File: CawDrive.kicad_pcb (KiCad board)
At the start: 4 copper layers, 40 x 40 mm, 81 parts, among them J1 Conn_01x11_Pin, J4 Conn_01x07_Pin, Q10 TPH3R704PL, Q11 TPH3R704PL, Q12 TPH3R704PL, Q7 TPH3R704PL, Q8 TPH3R704PL, Q9 TPH3R704PL, U1 STM32F446RETx, U2 TLV76733DRVR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

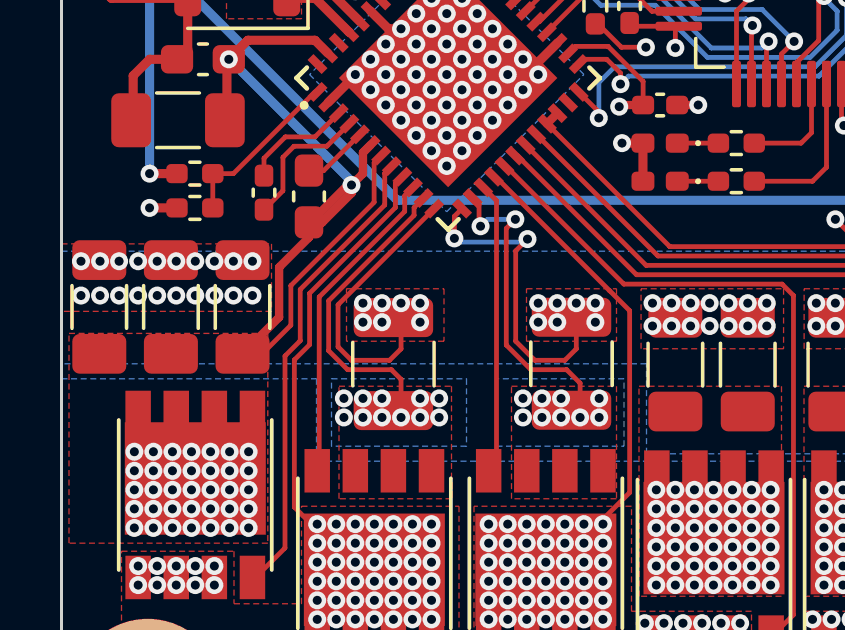
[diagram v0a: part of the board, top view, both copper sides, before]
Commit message: 优化底层丝印
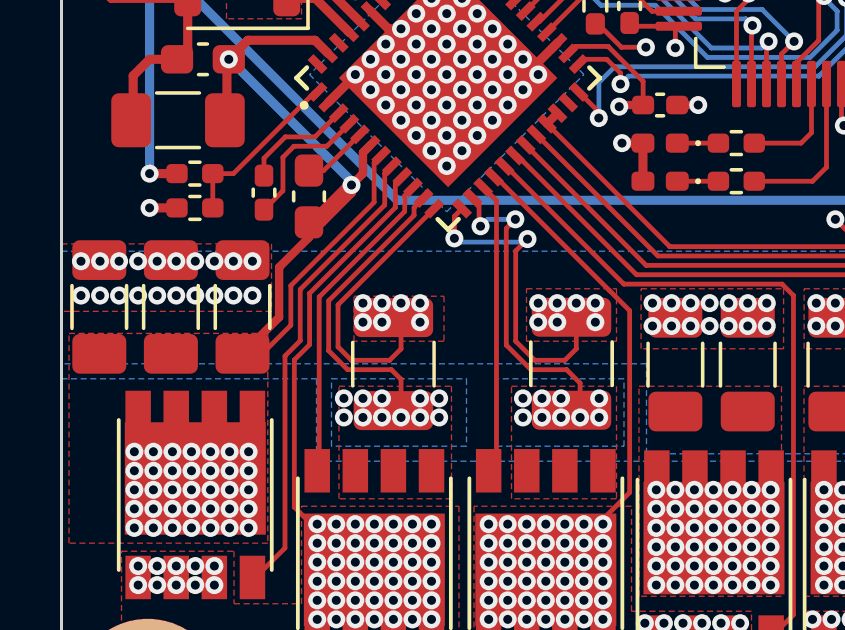
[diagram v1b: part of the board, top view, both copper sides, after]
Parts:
- removed the G*** at (154.0, 86.0)
- removed kibuzzard-6507110A: G***, kibuzzard-6507110A
- removed kibuzzard-650712D1: G***, kibuzzard-650712D1
- added G***: LOGO, Rick_Logo:guaik_logo_black_7x7, B.Cu at (156.0, 88.0)
- added kibuzzard-651AD87F: G***, kibuzzard-651AD87F, B.Cu at (121.5, 82.5)

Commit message: 优化布线
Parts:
- removed kibuzzard-65071EE4: G***, kibuzzard-65071EE4
- removed kibuzzard-650722D4: G***, kibuzzard-650722D4
- added C10: 0.1uF/50V, Capacitor_SMD:C_0402_1005Metric_Pad0.74x0.62mm_HandSolder, F.Cu at (158.5, 93.6)
- added D4: PWR_STA_LED, LED_SMD:LED_0402_1005Metric_Pad0.77x0.64mm_HandSolder, F.Cu at (138.0, 77.5)
- added R4: 0Ω, Resistor_SMD:R_0402_1005Metric_Pad0.72x0.64mm_HandSolder, F.Cu at (121.7, 90.8)
- added R7: 510, Resistor_SMD:R_0402_1005Metric_Pad0.72x0.64mm_HandSolder, F.Cu at (137.5, 75.7)
- added kibuzzard-651BBA97: G***, kibuzzard-651BBA97, B.Cu at (130.0, 78.0)
- R13: value 54.9k -> 54.9k ±0.1%
- R14: value 10k -> 10k ±0.1%
- R2: value 0 -> 0Ω
- moved R13 0.52 mm to (125.0, 89.7)
- moved R14 0.52 mm to (125.0, 90.8)
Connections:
- C20 pad 2: GND -> GND1
- C21 pad 2: GND -> GND1
- C22 pad 2: GND -> GND1
- C23 pad 2: GND -> GND1
- C24 pad 2: GND -> GND1
- C25 pad 2: GND -> GND1
- C26 pad 2: GND -> GND1
- C29 pad 2: GND -> GND1
- H8 pad 1: GND -> GND1
- Q12 pad 1: GND -> GND1
- Q12 pad 2: GND -> GND1
- Q12 pad 3: GND -> GND1
- R18 pad 2: GND -> GND1
- R19 pad 2: GND -> GND1
- TV1 pad 2: GND -> GND1
- U5 pad 12: GND -> GND1
- U5 pad 13: GND -> GND1
- U5 pad 21: GND -> GND1
- U5 pad 22: GND -> GND1
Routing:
- net GND1: track 0.00 -> 47.6 mm, vias 0 -> 53
- net GND: track 125.8 -> 79.1 mm, vias 144 -> 38
- net /DRV8323RSRGZR/PHASA: track 17.5 -> 13.5 mm, vias 52 -> 18
- net +3.3V: track 43.0 -> 39.2 mm
- net /DRV8323RSRGZR/PHASB: track 17.5 -> 13.9 mm, vias 54 -> 18
- net /DRV8323RSRGZR/PHASC: track 26.3 -> 23.5 mm, vias 47 -> 18
- net +36V: track 42.7 -> 44.8 mm, vias 121 -> 50
- net /USART2_RX: track 15.0 -> 13.5 mm
- net /SWDIO: track 23.7 -> 22.4 mm
- net /SWCLK: track 23.1 -> 21.8 mm
- net Net-(D4-K): track 0.00 -> 1.24 mm
- net /SPI3_MOSI: track 16.9 -> 16.3 mm
- net /ADC1_IN9: track 21.5 -> 22.0 mm
- net /DRV8323RSRGZR/FB: track 5.76 -> 5.24 mm
- net /DRV8323RSRGZR/SPB: track 10.6 -> 10.2 mm, vias 11 -> 10
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- added copper zone on In2.Cu, net +3.3V
- added copper zone on B.Cu, net GND1
- added copper zone on F.Cu, net GND1
- added copper zone on In1.Cu, net GND1
- added copper zone on In2.Cu, net GND1
- removed copper zone on In1.Cu, net +3.3V
- removed copper zone on F.Cu, net GND
- removed copper zone on In2.Cu, net GND
